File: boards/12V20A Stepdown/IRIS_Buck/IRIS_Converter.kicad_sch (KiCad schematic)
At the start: 27 parts, among them J1 TB005-762-02BE, J2 TB005-762-02BE, Q1 CSD17571Q2, Q2 CSD16340Q3, U1 LM25145RGYR

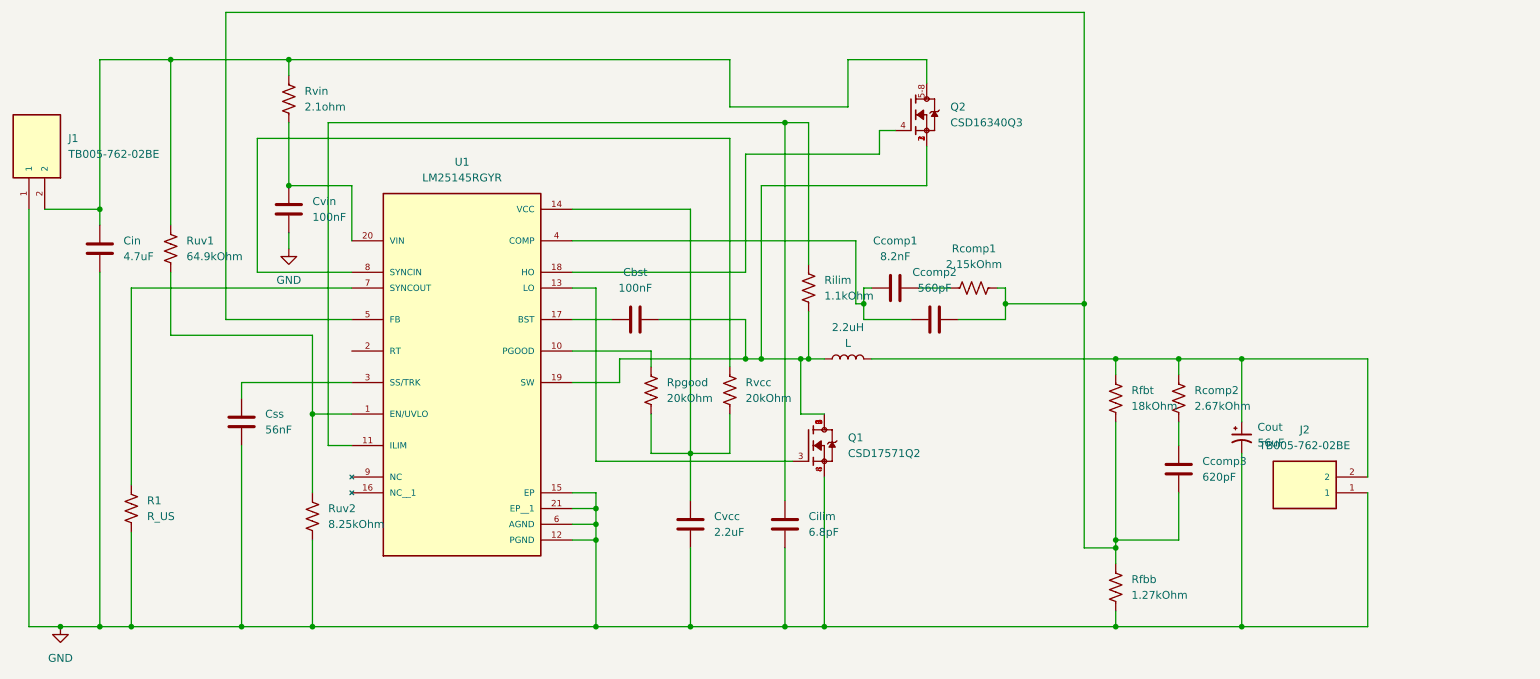
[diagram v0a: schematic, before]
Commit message: 10A board update on schematic
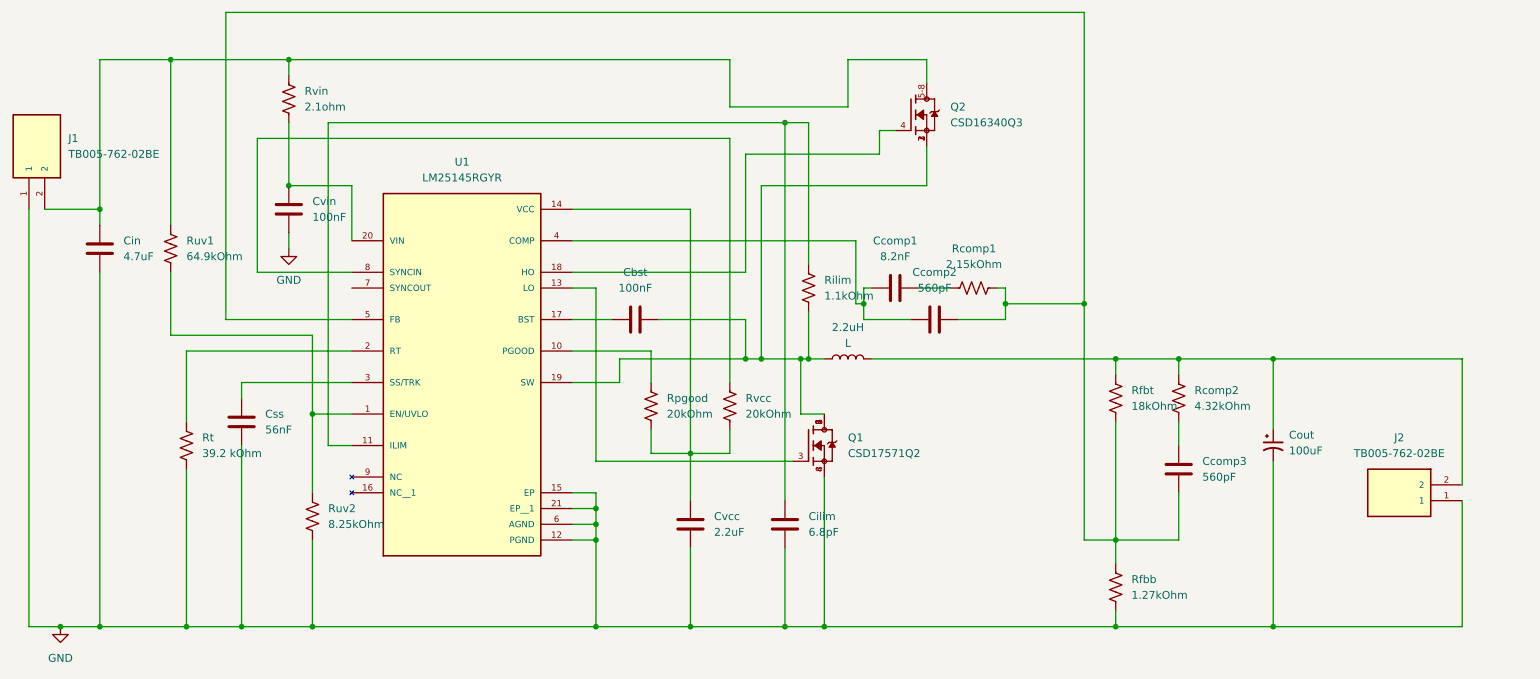
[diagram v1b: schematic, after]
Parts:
- removed R1: R_US, symbol Device:R_US
- added Rt: 39.2 kOhm, symbol Device:R_US
- Ccomp3: value 620pF -> 560pF
- Cout: value 56uF -> 100uF
- Rcomp2: value 2.67kOhm -> 4.32kOhm
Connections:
- net GND: now also Rt.2
- net at U1.2 (RT): now also Rt.1
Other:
- moved on the sheet: Cout, J2, Rpgood, Rvcc

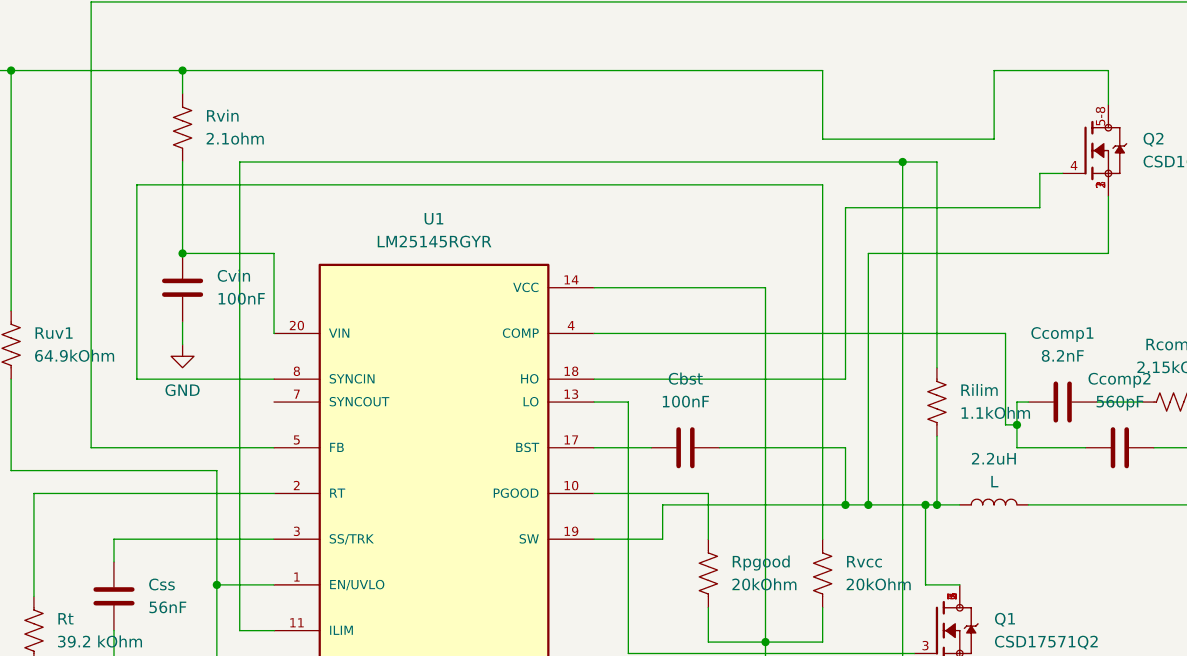
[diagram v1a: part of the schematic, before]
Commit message: 20A schematic validated and footprints added
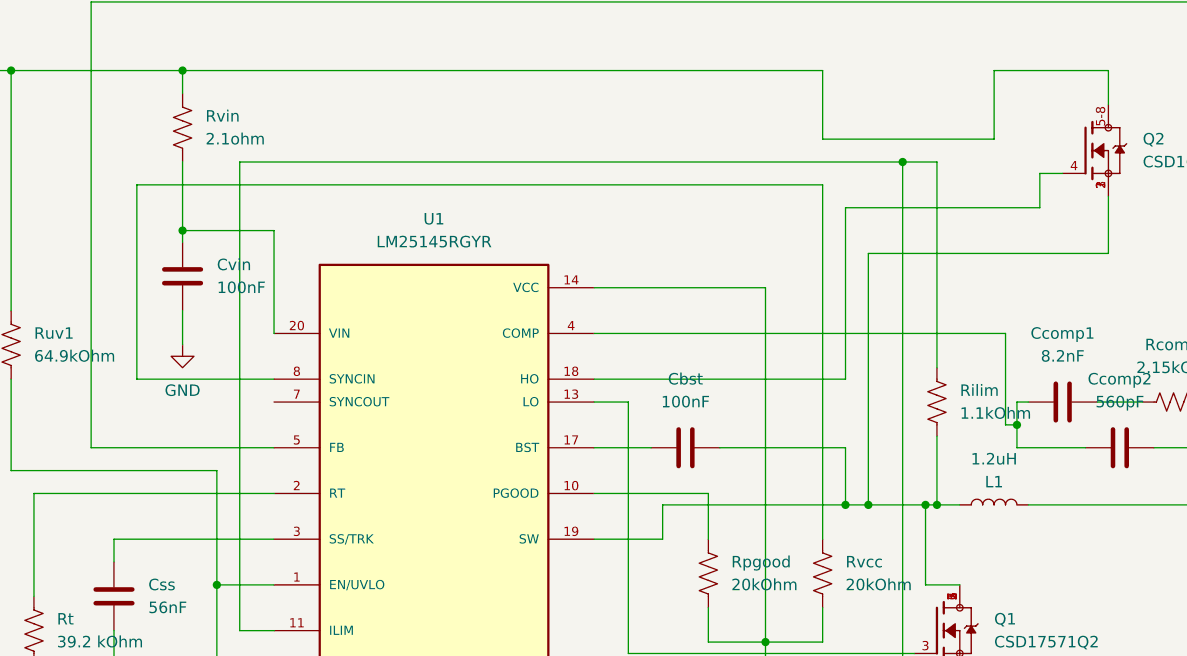
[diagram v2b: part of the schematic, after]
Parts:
- 1.2uH: renamed from 2.2uH; value L -> L1; footprint (none) -> 20A_Library:IND_IHLP_5050_FD_VIS
- Cbst, Cvin: footprint (none) -> 20A_Library:CAP_1608_TDK
- Ccomp1, Ccomp2, Ccomp3, Css: footprint (none) -> 20A_Library:G-155_MUR
- Cilim: footprint (none) -> 20A_Library:CAP_06031U0R5BAT2A
- Cin: footprint (none) -> 20A_Library:CAP_MSAS32-M_TAY
- Cout: footprint (none) -> 20A_Library:PCAP_SVP_E12_PAN
- Cvcc: footprint (none) -> 20A_Library:CAP_3216_TDK
- Rcomp1, Rilim, Rt: footprint (none) -> 20A_Library:RES_CRCW_0402
- Rcomp2, Rfbb, Ruv1, Rvin: footprint (none) -> 20A_Library:RC0402N_VIS
- Rfbt, Rpgood, Rvcc: footprint (none) -> 20A_Library:RC0603N_YAG
- Ruv2: footprint (none) -> 20A_Library:RES_CRCW_0603
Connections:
- net GND: now also Cvin.1; no longer Cvin.2
- net at Rvin.2, U1.20 (VIN): now also Cvin.2; no longer Cvin.1
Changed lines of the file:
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@@
 	)
 	(junction
+		(at 67.31 73.66)
+		(diameter 0)
+		(color 0 0 0 0)
+	)
+	(junction
 		(at 48.26 55.88)
 		(diameter 0)
@@
 	)
 	(junction
-		(at 67.31 76.2)
-		(diameter 0)
-		(color 0 0 0 0)
-	)
-	(junction
 		(at 36.83 147.32)
 		(diameter 0)
@@
 	(wire
 		(pts
+			(xy 67.31 73.66) (xy 67.31 74.93)
+		)
+		(stroke
+			(width 0)
+			(type default)
+		)
+	)
+	(wire
+		(pts
 			(xy 161.29 92.71) (xy 160.02 92.71)
 		)
@@
 	(wire
 		(pts
-			(xy 77.47 85.09) (xy 77.47 76.2)
+			(xy 77.47 85.09) (xy 77.47 73.66)
 		)
 		(stroke
@@
 	(wire
 		(pts
-			(xy 67.31 66.04) (xy 67.31 76.2)
+			(xy 67.31 66.04) (xy 67.31 73.66)
 		)
 		(stroke
@@
 	(wire
 		(pts
+			(xy 67.31 82.55) (xy 67.31 86.36)
+		)
+		(stroke
+			(width 0)
+			(type default)
+		)
+	)
+	(wire
+		(pts
 			(xy 147.32 66.04) (xy 147.32 127)
 		)
@@
 	(wire
 		(pts
-			(xy 77.47 76.2) (xy 67.31 76.2)
+			(xy 77.47 73.66) (xy 67.31 73.66)
 		)
 		(stroke
@@
 	(wire
 		(pts
-			(xy 67.31 83.82) (xy 67.31 86.36)
-		)
-		(stroke
-			(width 0)
-			(type default)
-		)
-	)
-	(wire
-		(pts
 			(xy 195.58 48.26) (xy 195.58 95.25)
 		)
@@
 			)
 		)
-		(property "Footprint" ""
+		(property "Footprint" "20A_Library:CAP_06031U0R5BAT2A"
 			(at 148.2852 134.62 0)
 			(effects
@@
 			)
 		)
-		(property "Footprint" ""
+		(property "Footprint" "20A_Library:RC0402N_VIS"
 			(at 49.276 86.614 90)
 			(effects
@@
 			)
 		)
-		(property "Footprint" ""
+		(property "Footprint" "20A_Library:RES_CRCW_0402"
 			(at 178.054 91.694 90)
 			(effects
@@
 			)
 		)
-		(property "Footprint" ""
+		(property "Footprint" "20A_Library:RES_CRCW_0603"
 			(at 72.136 129.794 90)
 			(effects
@@
 			)
 		)
-		(property "Footprint" ""
+		(property "Footprint" "20A_Library:G-155_MUR"
 			(at 175.26 96.8248 0)
 			(effects
@@
 			)
 		)
-		(property "Footprint" ""
+		(property "Footprint" "20A_Library:RC0402N_VIS"
 			(at 201.676 141.224 90)
 			(effects
@@
 			)
 		)
-		(property "Footprint" ""
+		(property "Footprint" "20A_Library:RES_CRCW_0402"
 			(at 51.816 118.364 90)
 			(effects
@@
 	)
 	(symbol
-		(lib_id "Device:C")
-		(at 67.31 80.01 0)
-		(unit 1)
-		(exclude_from_sim no)
-		(in_bom yes)
-		(on_board yes)
-		(dnp no)
-		(fields_autoplaced yes)
-		(property "Reference" "Cvin"
-			(at 71.12 78.7399 0)
-			(effects
-				(font
-					(size 1.27 1.27)
-				)
-				(justify left)
-			)
-		)
-		(property "Value" "100nF"
-			(at 71.12 81.2799 0)
-			(effects
-				(font
-					(size 1.27 1.27)
-				)
-				(justify left)
-			)
-		)
-		(property "Footprint" ""
-			(at 68.2752 83.82 0)
-			(effects
-				(font
-					(size 1.27 1.27)
-				)
-				(hide yes)
-			)
-		)
-		(property "Datasheet" "~"
-			(at 67.31 80.01 0)
-			(effects
-				(font
-					(size 1.27 1.27)
-				)
-				(hide yes)
-			)
-		)
-		(property "Description" "29.6mOhm"
-			(at 67.31 80.01 0)
-			(effects
-				(font
-					(size 1.27 1.27)
-				)
-				(hide yes)
-			)
-		)
-		(pin "2"
-		)
-		(pin "1"
-		)
-		(instances
-			(project "converter"
-				(path "/1513ce43-e5f2-482b-99a2-cdd75b9aa1c1"
-					(reference "Cvin")
-					(unit 1)
-				)
-			)
-		)
-	)
-	(symbol
 		(lib_id "TB005-762-02BE:TB005-762-02BE")
 		(at 246.38 124.46 180)
@@
 			)
 		)
-		(property "Footprint" ""
+		(property "Footprint" "20A_Library:G-155_MUR"
 			(at 211.7852 125.73 0)
 			(effects
@@
 			)
 		)
-		(property "Footprint" ""
+		(property "Footprint" "20A_Library:RC0603N_YAG"
 			(at 126.746 112.014 90)
 			(effects
@@
 			)
 		)
-		(property "Footprint" ""
+		(property "Footprint" "20A_Library:RC0402N_VIS"
 			(at 211.836 110.744 90)
 			(effects
@@
 		(dnp no)
 		(fields_autoplaced yes)
-		(property "Reference" "2.2uH"
+		(property "Reference" "1.2uH"
 			(at 157.48 99.06 90)
 			(effects
@@
 			)
 		)
-		(property "Value" "L"
+		(property "Value" "L1"
 			(at 157.48 101.6 90)
 			(effects
@@
 			)
 		)
-		(property "Footprint" ""
+		(property "Footprint" "20A_Library:IND_IHLP_5050_FD_VIS"
 			(at 157.48 104.14 0)
 			(effects
@@
 			(project ""
 				(path "/1513ce43-e5f2-482b-99a2-cdd75b9aa1c1"
-					(reference "2.2uH")
+					(reference "1.2uH")
 					(unit 1)
 				)
@@
 			)
 		)
-		(property "Footprint" ""
+		(property "Footprint" "20A_Library:G-155_MUR"
 			(at 168.91 91.7448 0)
 			(effects
@@
 			)
 		)
-		(property "Footprint" ""
+		(property "Footprint" "20A_Library:CAP_MSAS32-M_TAY"
 			(at 37.7952 90.17 0)
 			(effects
@@
 			)
 		)
-		(property "Footprint" ""
+		(property "Footprint" "20A_Library:CAP_3216_TDK"
 			(at 133.0452 134.62 0)
 			(effects
@@
 			)
 		)
-		(property "Footprint" ""
+		(property "Footprint" "20A_Library:G-155_MUR"
 			(at 60.6552 118.11 0)
 			(effects
@@
 			)
 		)
-		(property "Footprint" ""
+		(property "Footprint" "20A_Library:PCAP_SVP_E12_PAN"
 			(at 226.06 118.11 0)
 			(effects
@@
 			)
 		)
-		(property "Footprint" ""
+		(property "Footprint" "20A_Library:RC0402N_VIS"
 			(at 68.326 62.484 90)
 			(effects
@@
 			)
 		)
-		(property "Footprint" ""
+		(property "Footprint" "20A_Library:RC0603N_YAG"
 			(at 139.446 112.014 90)
 			(effects
@@
 			)
 		)
-		(property "Footprint" ""
+		(property "Footprint" "20A_Library:CAP_1608_TDK"
 			(at 127 96.8248 0)
 			(effects
@@
 			)
 		)
-		(property "Footprint" ""
+		(property "Footprint" "20A_Library:RC0603N_YAG"
 			(at 201.676 110.744 90)
 			(effects
@@
 	)
 	(symbol
+		(lib_id "Device:C")
+		(at 67.31 78.74 180)
+		(unit 1)
+		(exclude_from_sim no)
+		(in_bom yes)
+		(on_board yes)
+		(dnp no)
+		(fields_autoplaced yes)
+		(property "Reference" "Cvin"
+			(at 71.12 77.4699 0)
+			(effects
+				(font
+					(size 1.27 1.27)
+				)
+				(justify right)
+			)
+		)
+		(property "Value" "100nF"
+			(at 71.12 80.0099 0)
+			(effects
+				(font
+					(size 1.27 1.27)
+				)
+				(justify right)
+			)
+		)
+		(property "Footprint" "20A_Library:CAP_1608_TDK"
+			(at 66.3448 74.93 0)
+			(effects
+				(font
+					(size 1.27 1.27)
+				)
+				(hide yes)
+			)
+		)
+		(property "Datasheet" "~"
+			(at 67.31 78.74 0)
+			(effects
+				(font
+					(size 1.27 1.27)
+				)
+				(hide yes)
+			)
+		)
+		(property "Description" "Unpolarized capacitor"
+			(at 67.31 78.74 0)
+			(effects
+				(font
+					(size 1.27 1.27)
+				)
+				(hide yes)
+			)
+		)
+		(pin "2"
+		)
+		(pin "1"
+		)
+		(instances
+			(project "IRIS_Converter"
+				(path "/1513ce43-e5f2-482b-99a2-cdd75b9aa1c1"
+					(reference "Cvin")
+					(unit 1)
+				)
+			)
+		)
+	)
+	(symbol
 		(lib_id "Device:R_US")
 		(at 151.13 92.71 0)
@@
 		(exclude_from_sim no)
 		(in_bom yes)
-		(on_board yes)
+		(on_board no)
 		(dnp no)
 		(property "Reference" "Rilim"
@@
 			)
 		)
-		(property "Footprint" ""
+		(property "Footprint" "20A_Library:RES_CRCW_0402"
 			(at 152.146 92.964 90)
 			(effects
